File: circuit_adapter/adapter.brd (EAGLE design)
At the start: 100 x 80 mm, 3 parts, among them CN1 5035521020, X1 2510-

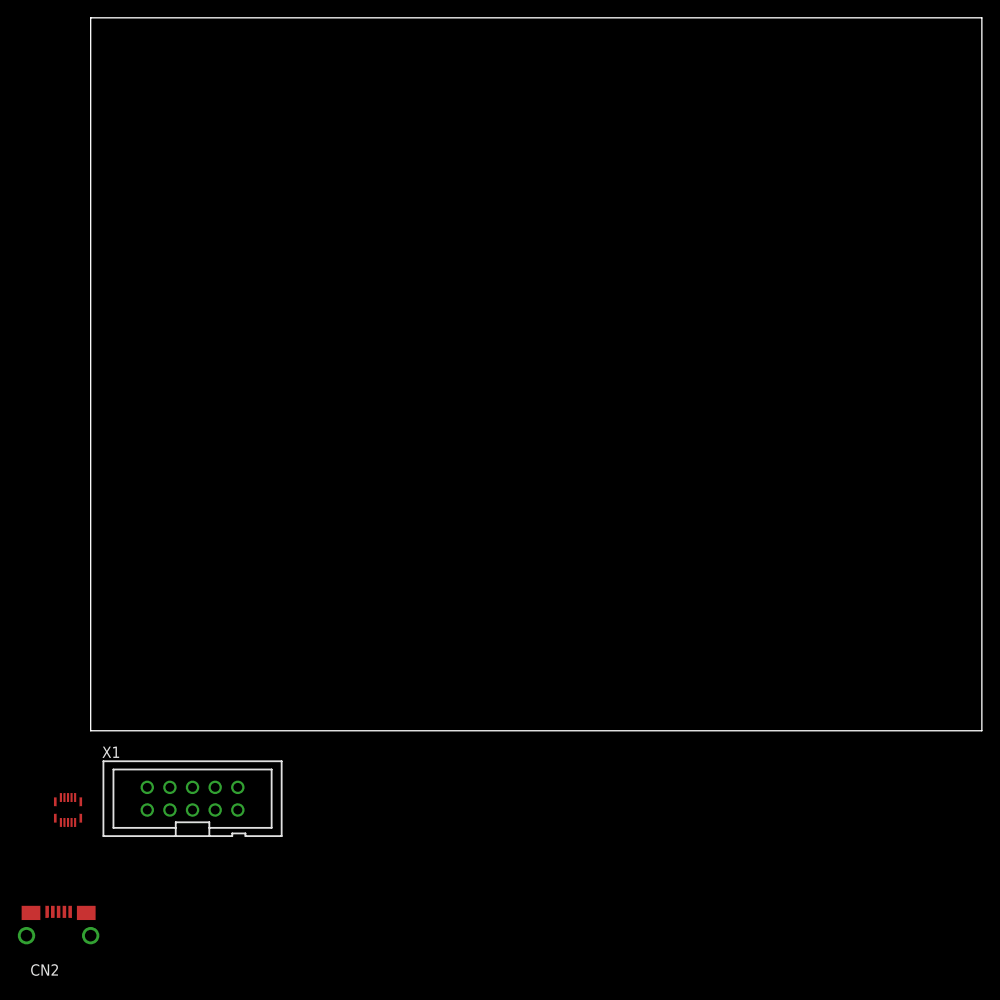
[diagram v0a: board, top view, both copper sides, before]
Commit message: Modified adapter circuit
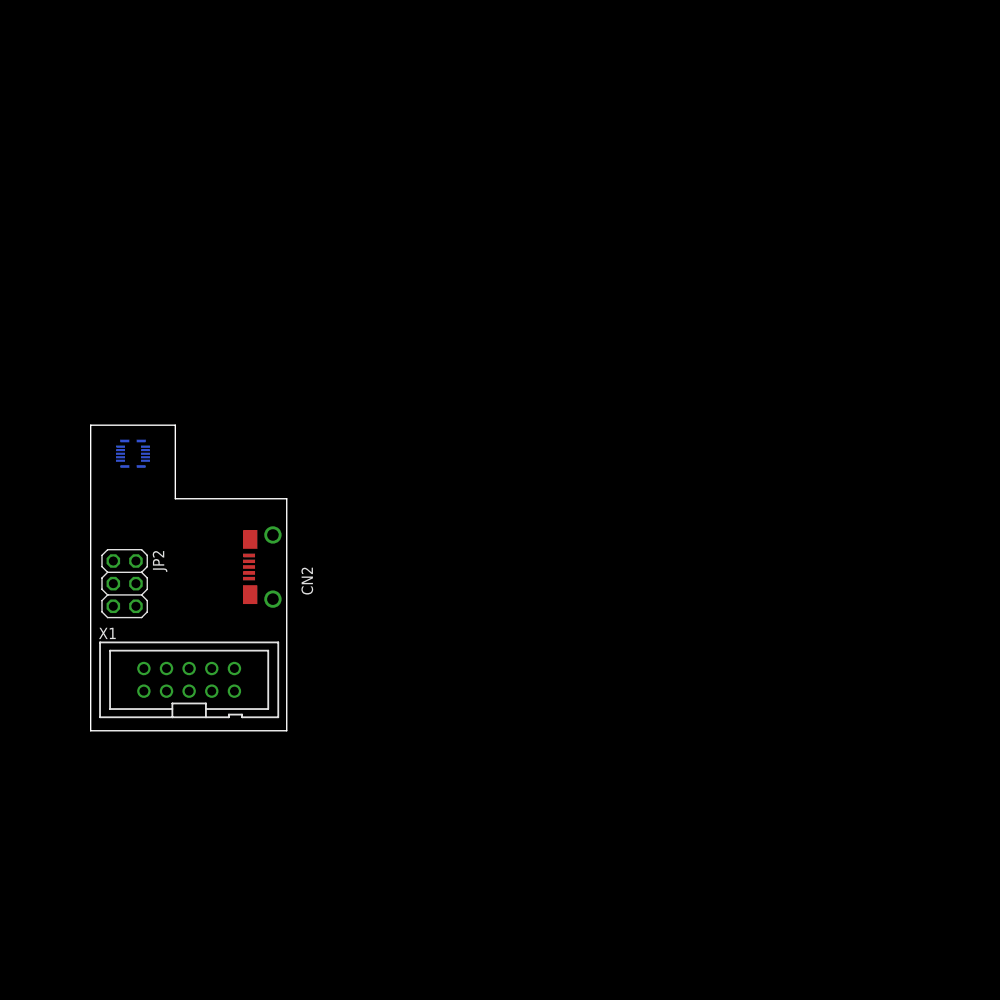
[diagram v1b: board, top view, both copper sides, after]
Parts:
- added JP2: (no value), pinhead:2X03
- moved CN2 47.8 mm to (20.4, 18.4), turned to 90 degrees
- moved CN1 40.6 mm to (4.75, 31.1), flipped to the bottom, turned to 90 degrees
- moved X1 13.3 mm to (11.0, 5.71)
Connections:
- new net N$1: CN1.2, JP2.3
- new net N$2: CN1.4, JP2.5
- new net N$3: CN1.6, JP2.6
- new net N$4: CN1.8, JP2.4
- net DGND: now also JP2.2
- net VBUS: now also JP2.1
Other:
- board size 100 x 80 mm -> 22 x 34.3 mm

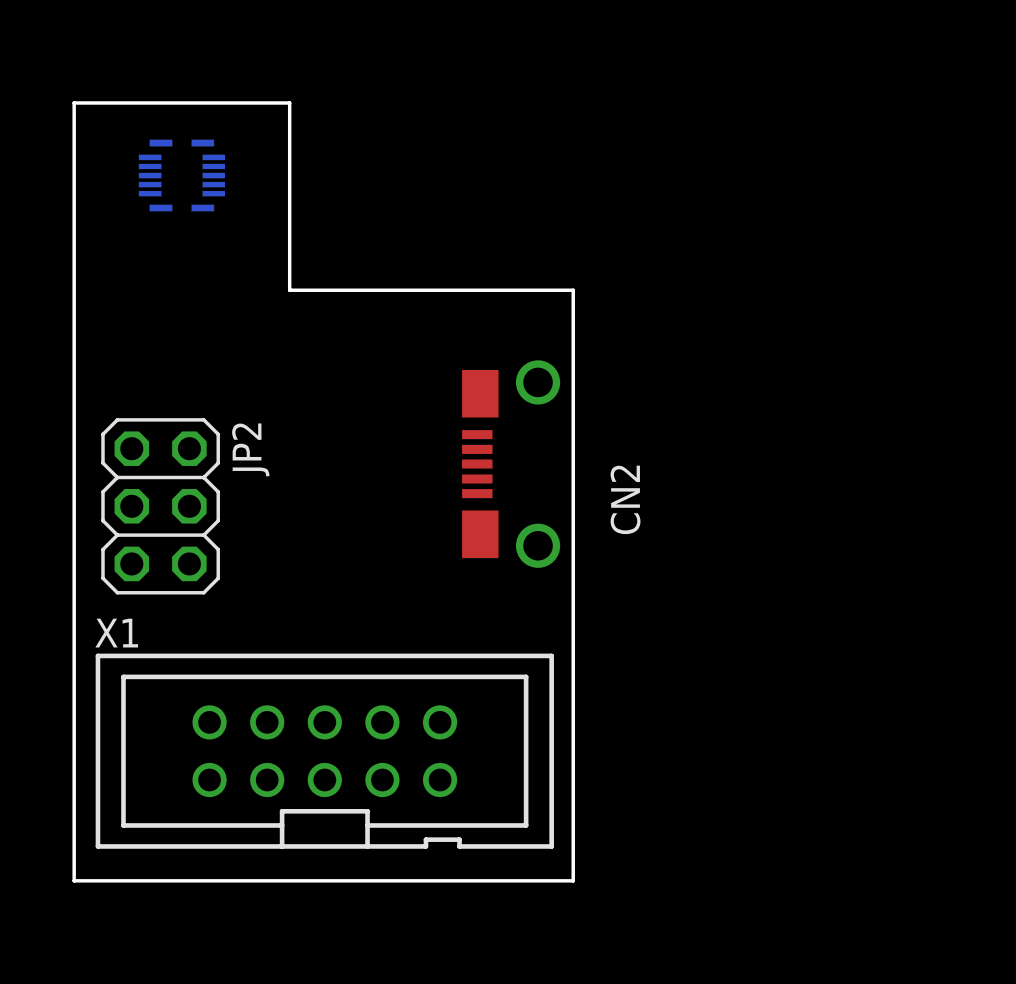
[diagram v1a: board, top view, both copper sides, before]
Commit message: Modified adapter circuit
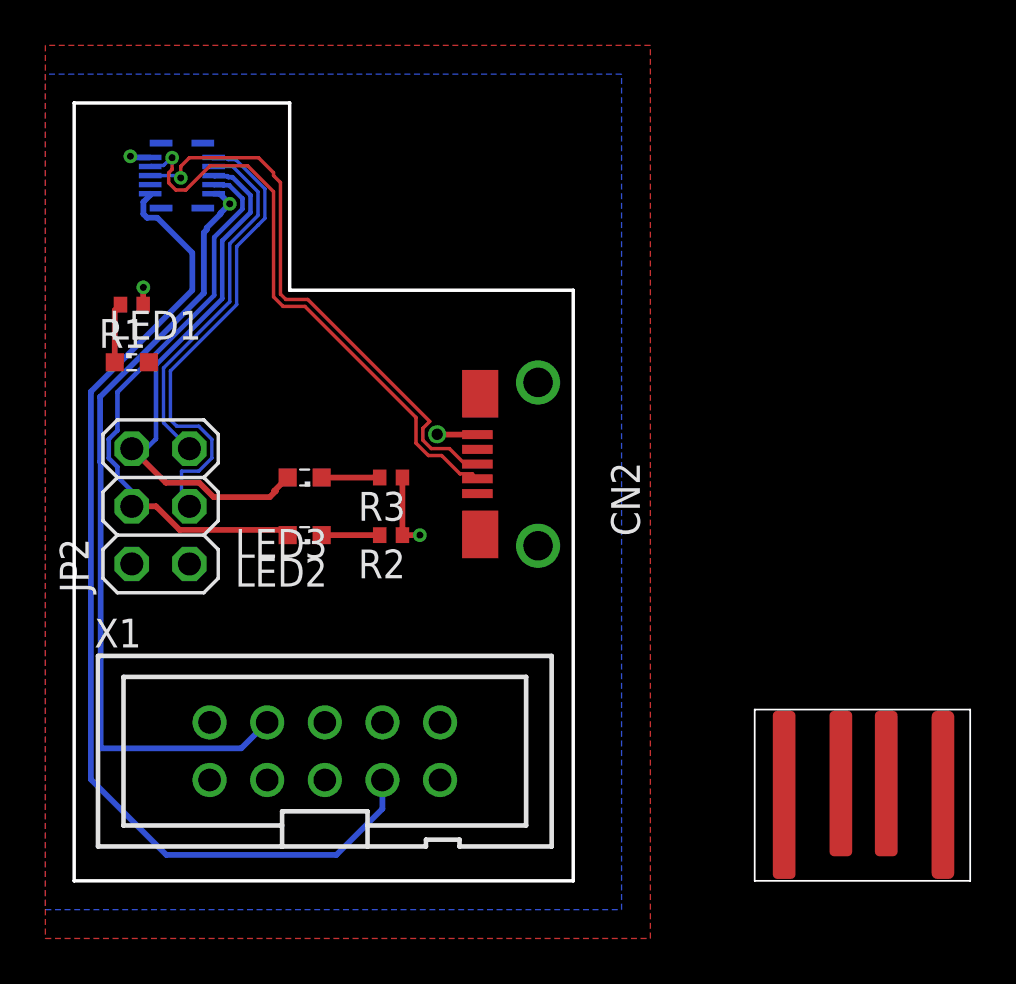
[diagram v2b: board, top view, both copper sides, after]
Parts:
- added CN3: USB_BARE, connector:USB_BARE
- added LED1, LED2, LED3: (no value), led:SML0603
- added R1, R3: 5.1k, rcl:R0402
- added R2: 5.1, rcl:R0402
- turned JP2 to 90 degrees
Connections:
- net N$1 renamed TX1
- net N$2 renamed RX1
- removed net DGND: JP2.2, X1.2, X1.3, X1.9
- removed net N$4: CN1.8, JP2.4
- new net GPIO0: CN1.8, JP2.4, LED2.A
- new net GPIO1: CN1.6, JP2.6, LED3.A
- new net N$1: LED1.C, R1.2
- new net N$2: LED2.C, R2.2
- net GND: now also JP2.2, R1.1, R2.1, R3.1, X1.2, X1.3, X1.9
- net N$3: now also LED3.C, R3.2; no longer CN1.6, JP2.6
- net VBUS: now also LED1.A
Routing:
- net C2CK: track 0.00 -> 45.3 mm
- net C2D: track 0.00 -> 35.1 mm, vias 0 -> 1
- net D-: track 0.00 -> 25.6 mm, vias 0 -> 1
- net GPIO0: track 0.00 -> 25.3 mm
- net D+: track 0.00 -> 24.6 mm, vias 0 -> 1
- net GPIO1: track 0.00 -> 24.2 mm
- net TX1: track 0.00 -> 21.1 mm
- net RX1: track 0.00 -> 15.9 mm
- net GND: track 0.00 -> 5.85 mm, vias 0 -> 3
- net N$1: track 0.00 -> 2.64 mm
- net N$3: track 0.00 -> 2.56 mm
- net N$2: track 0.00 -> 2.56 mm
- net VBUS: track 0.00 -> 0.89 mm, vias 0 -> 1
- added copper zone on layer 16, net GND
- added copper zone on layer 1, net VBUS
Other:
- board size 22 x 34.3 mm -> 39.5 x 34.3 mm

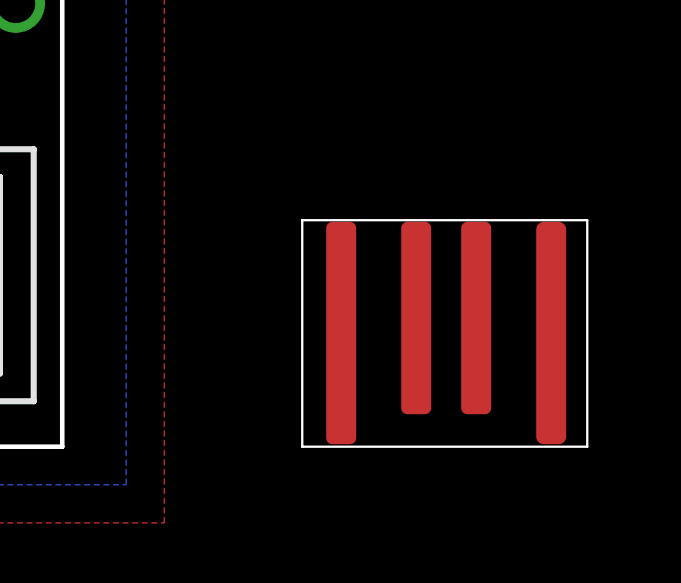
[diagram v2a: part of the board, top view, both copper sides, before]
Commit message: Modified adapter circuit
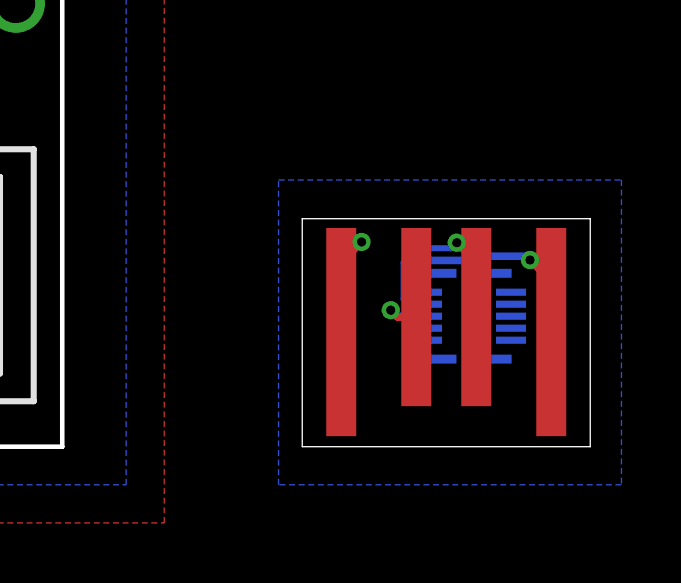
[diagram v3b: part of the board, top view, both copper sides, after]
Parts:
- added CN4: (no value), connector:USB
- CN3: value USB_BARE -> 5035521020; device connector:USB_BARE -> connector:5035521020
- moved CN3 3.23 mm to (35.6, 4.35), flipped to the bottom, turned to 90 degrees
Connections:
- new net D+2: CN3.5, CN4.D+
- new net D-2: CN3.3, CN4.D-
- new net GND2: CN3.7, CN4.GND
- new net VBUS2: CN3.1, CN4.VBUS
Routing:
- net VBUS2: track 0.00 -> 7.62 mm, vias 0 -> 1
- net D-2: track 0.00 -> 6.87 mm, vias 0 -> 1
- net GND2: track 0.00 -> 3.29 mm, vias 0 -> 1
- net D+2: track 0.00 -> 2.24 mm, vias 0 -> 1
- added copper zone on layer 16, net GND2
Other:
- board size 39.5 x 34.3 mm -> 39.6 x 34.3 mm
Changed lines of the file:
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@@
 <setting verticaltext="up"/>
 </settings>
-<grid distance="50" unitdist="mil" unit="mm" style="lines" multiple="1" display="no" altdistance="5" altunitdist="mil" altunit="mm"/>
+<grid distance="50" unitdist="mil" unit="mm" style="lines" multiple="1" display="no" altdistance="0.05" altunitdist="mm" altunit="mm"/>
 <layers>
 <layer number="1" name="Top" color="4" fill="1" visible="yes" active="yes"/>
@@
 <wire x1="22" y1="0" x2="0" y2="0" width="0.1524" layer="20"/>
 <wire x1="-2.54" y1="26.74" x2="12.7" y2="26.74" width="0.0762" layer="51" style="shortdash"/>
-<wire x1="30" y1="7.55" x2="39.5" y2="7.55" width="0.0762" layer="20"/>
-<wire x1="39.5" y1="7.55" x2="39.5" y2="0" width="0.0762" layer="20"/>
-<wire x1="39.5" y1="0" x2="30" y2="0" width="0.0762" layer="20"/>
-<wire x1="30" y1="0" x2="30" y2="7.55" width="0.0762" layer="20"/>
+<wire x1="30" y1="7.6" x2="39.6" y2="7.6" width="0.01" layer="20"/>
+<wire x1="39.6" y1="7.6" x2="39.6" y2="0" width="0.01" layer="20"/>
+<wire x1="39.6" y1="0" x2="30" y2="0" width="0.01" layer="20"/>
+<wire x1="30" y1="0" x2="30" y2="7.6" width="0.01" layer="20"/>
 </plain>
 <attributes>
@@
 <attribute name="VALUE" x="14.605" y="19.685" size="1.27" layer="27" rot="R180"/>
 </element>
-<element name="CN3" library="connector" package="USB_BARE" value="USB_BARE" x="34.798" y="7.493"/>
+<element name="CN4" library="connector" package="USB" value="" x="31.3" y="3.82"/>
+<element name="CN3" library="connector" package="5035521020" value="5035521020" x="35.56" y="4.35" rot="MR90"/>
 </elements>
 <signals>
@@
 <wire x1="13.47" y1="17.78" x2="10.91" y2="17.78" width="0.254" layer="1"/>
 </signal>
+<signal name="VBUS2">
+<contactref element="CN4" pad="VBUS"/>
+<contactref element="CN3" pad="1"/>
+<wire x1="37.465" y1="6.35" x2="37.592" y2="6.223" width="0.254" layer="16"/>
+<via x="37.592" y="6.223" extent="1-16" drill="0.3048"/>
+<wire x1="37.592" y1="6.223" x2="38.3" y2="5.515" width="0.254" layer="1"/>
+<wire x1="38.3" y1="5.515" x2="38.3" y2="3.82" width="0.254" layer="1"/>
+<wire x1="33.8606" y1="6.04573125" x2="34.02426875" y2="6.2094" width="0.254" layer="16"/>
+<wire x1="34.16" y1="5.157" x2="33.8606" y2="5.4564" width="0.254" layer="16"/>
+<wire x1="33.8606" y1="5.4564" x2="33.8606" y2="6.04573125" width="0.254" layer="16"/>
+<wire x1="35.5261875" y1="6.35" x2="37.465" y2="6.35" width="0.254" layer="16"/>
+<wire x1="34.02426875" y1="6.2094" x2="35.3855875" y2="6.2094" width="0.254" layer="16"/>
+<wire x1="35.3855875" y1="6.2094" x2="35.5261875" y2="6.35" width="0.254" layer="16"/>
+<wire x1="34.16" y1="5.157" x2="34.16" y2="5.15" width="0" layer="19" extent="16-16"/>
+</signal>
+<signal name="D-2" class="1">
+<contactref element="CN4" pad="D-"/>
+<contactref element="CN3" pad="3"/>
+<wire x1="33.54426875" y1="4.7506" x2="33.3806" y2="4.91426875" width="0.2032" layer="16"/>
+<wire x1="34.16" y1="4.75" x2="34.1594" y2="4.7506" width="0.2032" layer="16"/>
+<wire x1="34.1594" y1="4.7506" x2="33.54426875" y2="4.7506" width="0.2032" layer="16"/>
+<wire x1="33.3806" y1="4.91426875" x2="33.3806" y2="6.14046875" width="0.2032" layer="16"/>
+<wire x1="33.3806" y1="6.14046875" x2="33.85593125" y2="6.6158" width="0.2032" layer="16"/>
+<wire x1="34.9658" y1="6.6158" x2="35.15" y2="6.8" width="0.2032" layer="16"/>
+<via x="35.15" y="6.8" extent="1-16" drill="0.3048"/>
+<wire x1="33.85593125" y1="6.6158" x2="34.9658" y2="6.6158" width="0.2032" layer="16"/>
+<wire x1="35.15" y1="6.8" x2="35.8" y2="6.15" width="0.254" layer="1"/>
+<wire x1="35.8" y1="6.15" x2="35.8" y2="4.32" width="0.254" layer="1"/>
+</signal>
+<signal name="D+2">
+<contactref element="CN4" pad="D+"/>
+<contactref element="CN3" pad="5"/>
+<wire x1="33.8" y1="4.32" x2="33.18" y2="4.32" width="0.254" layer="1"/>
+<wire x1="33.18" y1="4.32" x2="32.95" y2="4.55" width="0.254" layer="1"/>
+<via x="32.95" y="4.55" extent="1-16" drill="0.3048"/>
+<wire x1="34.16" y1="4.35" x2="33.15" y2="4.35" width="0.254" layer="16"/>
+<wire x1="33.15" y1="4.35" x2="32.95" y2="4.55" width="0.254" layer="16"/>
+</signal>
+<signal name="GND2">
+<contactref element="CN4" pad="GND"/>
+<contactref element="CN3" pad="7"/>
+<wire x1="31.977" y1="6.827" x2="31.3" y2="6.15" width="0.254" layer="1"/>
+<wire x1="31.3" y1="3.82" x2="31.3" y2="6.15" width="0.254" layer="1"/>
+<via x="31.977" y="6.827" extent="1-16" drill="0.3048"/>
+<polygon width="0.15" layer="16">
+<vertex x="29.21" y="8.89"/>
+<vertex x="40.64" y="8.89"/>
+<vertex x="40.64" y="-1.27"/>
+<vertex x="29.21" y="-1.27"/>
+</polygon>
+</signal>
 </signals>

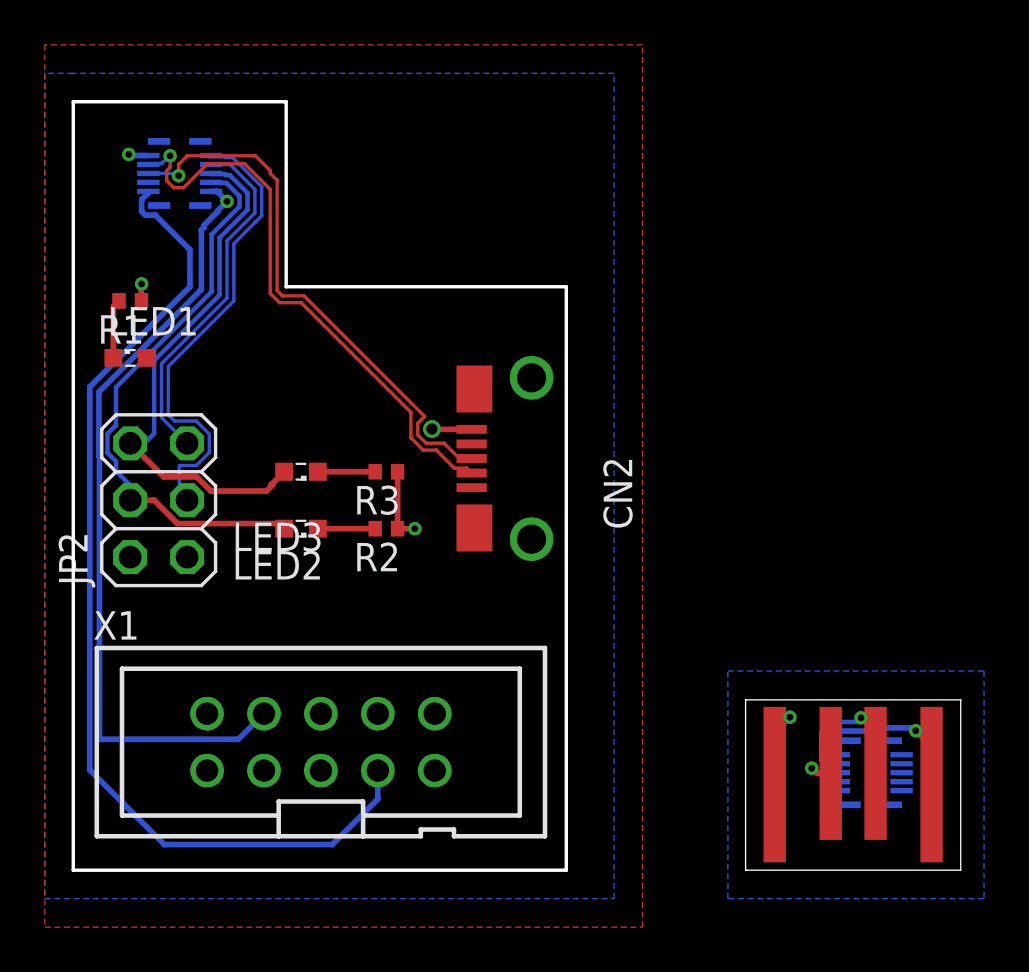
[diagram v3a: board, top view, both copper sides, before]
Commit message: Modified adapter circuit
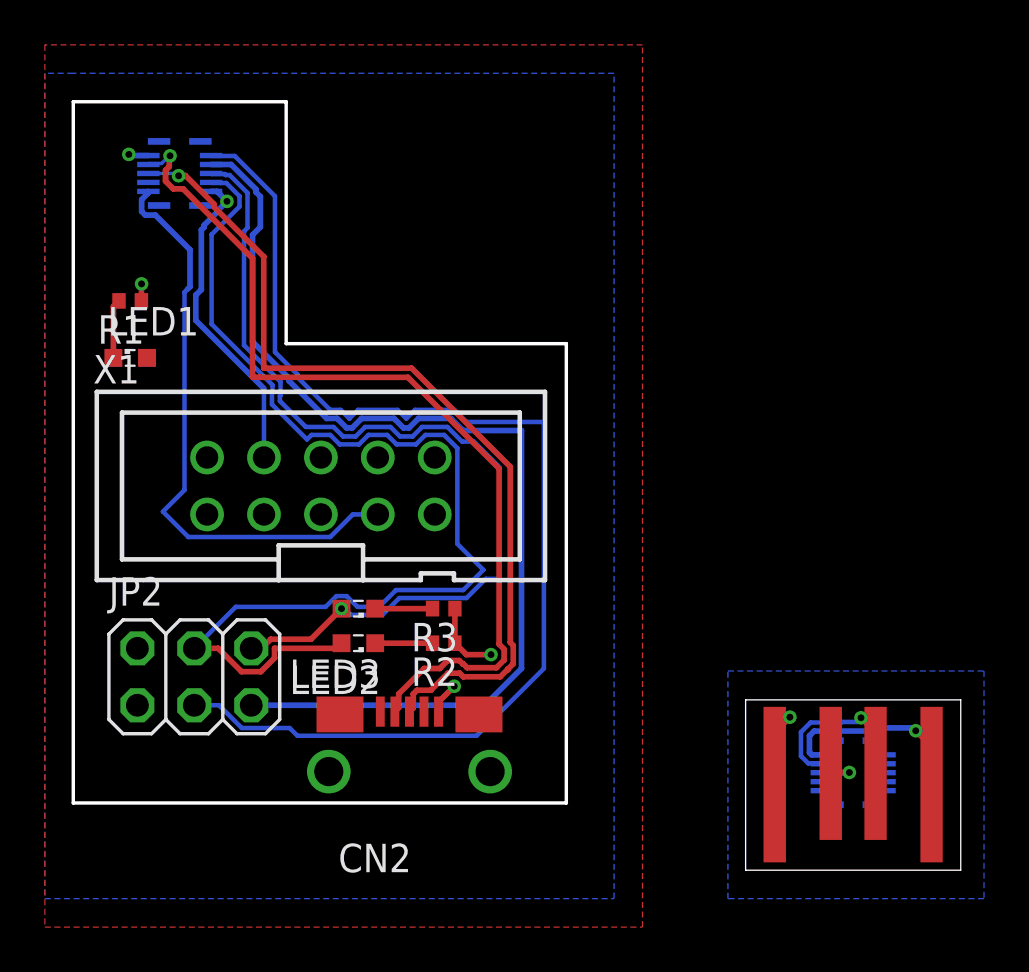
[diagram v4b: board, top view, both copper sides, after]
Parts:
- moved CN2 15.0 mm to (15.0, 4.40), turned to 0 degrees
- moved X1 11.4 mm to (11.0, 17.1)
- moved JP2 8.04 mm to (5.40, 8.63), turned to 0 degrees
- moved LED3 6.62 mm to (12.7, 11.7)
- moved R3 6.62 mm to (16.5, 11.7)
- moved LED2 5.72 mm to (12.7, 10.1)
- moved R2 5.72 mm to (16.5, 10.1)
- moved CN3 0.76 mm to (34.8, 4.35)
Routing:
- net TX1: track 21.1 -> 53.0 mm
- net RX1: track 15.9 -> 47.3 mm
- net GPIO0: track 25.3 -> 50.9 mm
- net C2D: track 35.1 -> 14.2 mm
- net C2CK: track 45.3 -> 26.5 mm
- net D-: track 25.6 -> 42.8 mm
- net GPIO1: track 24.2 -> 41.3 mm, vias 0 -> 1
- net D+: track 24.6 -> 39.4 mm
- net VBUS2: track 7.62 -> 8.98 mm
- net D-2: track 6.87 -> 7.83 mm
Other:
- outline, holes or cut-outs redrawn
